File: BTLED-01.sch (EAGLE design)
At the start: 17 parts

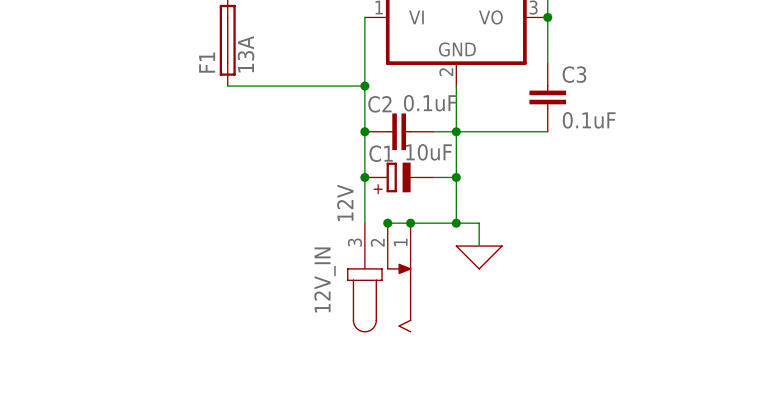
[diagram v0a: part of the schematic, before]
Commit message: feat: Replaced DC input jack with Wago screw terminals
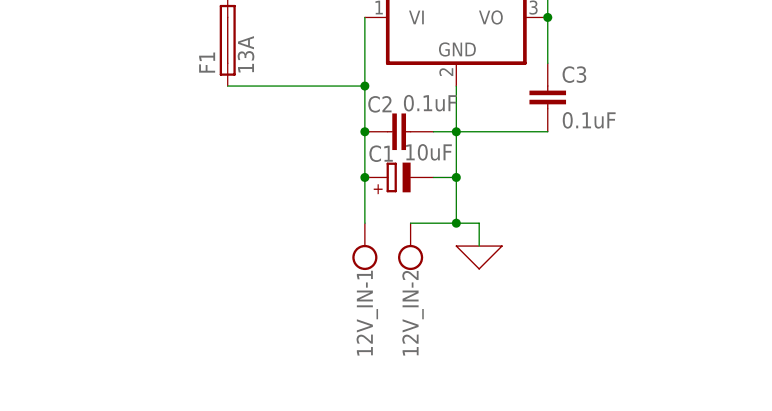
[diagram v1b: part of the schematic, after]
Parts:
- 12V_IN: value 12V -> (none); device con-jack:JACK-PLUG1 -> con-wago-500:W237-102
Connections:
- net 12V_IN: now also 12V_IN-1.KL; no longer 12V_IN.3
- net GND: now also 12V_IN-2.KL; no longer 12V_IN.1, 12V_IN.2
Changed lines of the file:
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@@
 <part name="FET_G" library="transistor-power" library_urn="urn:adsk.eagle:library:400" deviceset="IRF540" device="" package3d_urn="urn:adsk.eagle:package:29484/3"/>
 <part name="LED_OUT" library="con-wago-500" library_urn="urn:adsk.eagle:library:195" deviceset="W237-4" device="" package3d_urn="urn:adsk.eagle:package:10695/1"/>
-<part name="12V_IN" library="con-jack" library_urn="urn:adsk.eagle:library:154" deviceset="JACK-PLUG" device="1" package3d_urn="urn:adsk.eagle:package:7494/1" value="12V"/>
 <part name="5V_REG" library="linear" library_urn="urn:adsk.eagle:library:262" deviceset="78*" device="TV" package3d_urn="urn:adsk.eagle:package:16417/2" technology="05"/>
 <part name="X_5" library="ngspice-simulation" library_urn="urn:adsk.eagle:library:527439" deviceset="GND" device=""/>
@@
 <part name="R4" library="rcl" library_urn="urn:adsk.eagle:library:334" deviceset="R-EU_" device="0204/7" package3d_urn="urn:adsk.eagle:package:23498/2" value="100"/>
 <part name="R5" library="rcl" library_urn="urn:adsk.eagle:library:334" deviceset="R-EU_" device="0204/7" package3d_urn="urn:adsk.eagle:package:23498/2" value="100"/>
+<part name="12V_IN" library="con-wago-500" library_urn="urn:adsk.eagle:library:195" deviceset="W237-102" device="" package3d_urn="urn:adsk.eagle:package:10688/1"/>
 </parts>
 <sheets>
@@
 <attribute name="NAME" x="-12.7" y="18.669" size="1.778" layer="95" rot="R180"/>
 </instance>
-<instance part="12V_IN" gate="G$1" x="12.7" y="-22.86" smashed="yes" rot="R90">
-<attribute name="NAME" x="6.35" y="-27.94" size="1.778" layer="95" rot="R90"/>
-<attribute name="VALUE" x="8.89" y="-17.78" size="1.778" layer="96" rot="R90"/>
-</instance>
 <instance part="5V_REG" gate="A1" x="20.32" y="5.08" smashed="yes">
 <attribute name="NAME" x="10.16" y="8.255" size="1.778" layer="95"/>
@@
 <attribute name="NAME" x="31.75" y="72.6186" size="1.778" layer="95"/>
 <attribute name="VALUE" x="36.83" y="72.644" size="1.778" layer="96"/>
+</instance>
+<instance part="12V_IN" gate="-1" x="10.16" y="-22.86" smashed="yes" rot="R90">
+<attribute name="NAME" x="9.271" y="-22.86" size="1.778" layer="95" rot="R270"/>
+</instance>
+<instance part="12V_IN" gate="-2" x="15.24" y="-22.86" smashed="yes" rot="R90">
+<attribute name="VALUE" x="18.923" y="-25.4" size="1.778" layer="96" rot="R90"/>
+<attribute name="NAME" x="14.351" y="-22.86" size="1.778" layer="95" rot="R270"/>
 </instance>
 </instances>
@@
 <net name="GND" class="0">
 <segment>
-<pinref part="12V_IN" gate="G$1" pin="1"/>
 <wire x1="15.24" y1="-17.78" x2="20.32" y2="-17.78" width="0.1524" layer="91"/>
 <wire x1="20.32" y1="-17.78" x2="20.32" y2="-12.7" width="0.1524" layer="91"/>
@@
 <pinref part="C3" gate="G$1" pin="2"/>
 <wire x1="30.48" y1="-7.62" x2="20.32" y2="-7.62" width="0.1524" layer="91"/>
-<pinref part="12V_IN" gate="G$1" pin="2"/>
-<junction x="12.7" y="-17.78"/>
-<wire x1="12.7" y1="-17.78" x2="15.24" y2="-17.78" width="0.1524" layer="91"/>
-<junction x="15.24" y="-17.78"/>
 <pinref part="5V_REG" gate="A1" pin="GND"/>
 <wire x1="20.32" y1="-2.54" x2="20.32" y2="-7.62" width="0.1524" layer="91"/>
+<pinref part="12V_IN" gate="-2" pin="KL"/>
 </segment>
 <segment>
@@
 <segment>
 <pinref part="F1" gate="1" pin="1"/>
-<pinref part="12V_IN" gate="G$1" pin="3"/>
 <wire x1="-5.08" y1="-2.54" x2="10.16" y2="-2.54" width="0.1524" layer="91"/>
 <wire x1="10.16" y1="-2.54" x2="10.16" y2="-7.62" width="0.1524" layer="91"/>
@@
 <wire x1="10.16" y1="5.08" x2="10.16" y2="-2.54" width="0.1524" layer="91"/>
 <junction x="10.16" y="-2.54"/>
-</segment>
-</net>
+<pinref part="12V_IN" gate="-1" pin="KL"/>
+</segment>
+</net>
